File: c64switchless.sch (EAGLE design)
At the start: 12 parts, among them IC1 27C256, IC2 PIC12F629P

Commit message: hole sizes
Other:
- note added: "Rev 1.12"
- note removed: "Rev 1.11"
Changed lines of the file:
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@@
 <text x="165.1" y="17.78" size="1.778" layer="91">adapter with switchless multikernal switch</text>
 <text x="165.1" y="12.7" size="1.778" layer="91">Design by BWACK</text>
-<text x="246.634" y="5.334" size="1.778" layer="91">Rev 1.11</text>
+<text x="246.634" y="5.334" size="1.778" layer="91">Rev 1.12</text>
 <text x="165.1" y="5.08" size="1.778" layer="91">http://www.ohwr.org/</text>
 <text x="165.1" y="7.62" size="1.778" layer="91">CERN OPEN HARDWARE LICENSE v1.2</text>

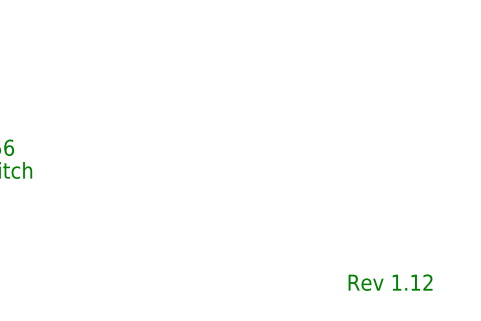
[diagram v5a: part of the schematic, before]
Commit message: Rev 1.13
Moved IC2 to clear space for the socket in the C64.
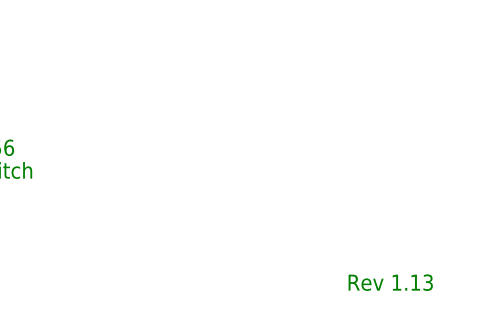
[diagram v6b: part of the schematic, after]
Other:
- note added: "Rev 1.13"
- note removed: "Rev 1.12"
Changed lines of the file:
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@@
 <text x="165.1" y="17.78" size="1.778" layer="91">adapter with switchless multikernal switch</text>
 <text x="165.1" y="12.7" size="1.778" layer="91">Design by BWACK</text>
-<text x="246.634" y="5.334" size="1.778" layer="91">Rev 1.12</text>
+<text x="246.634" y="5.334" size="1.778" layer="91">Rev 1.13</text>
 <text x="165.1" y="5.08" size="1.778" layer="91">http://www.ohwr.org/</text>
 <text x="165.1" y="7.62" size="1.778" layer="91">CERN OPEN HARDWARE LICENSE v1.2</text>

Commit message: resistor values
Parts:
- R1: value 2k -> 1k
- R2: value 2k -> 3k3
- R3: value 2k -> 560R
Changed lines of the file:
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@@
 <part name="GND5" library="supply1" deviceset="GND" device=""/>
 <part name="GND6" library="supply1" deviceset="GND" device=""/>
-<part name="R1" library="rcl" deviceset="R-EU_" device="0207/10" value="2k"/>
-<part name="R2" library="rcl" deviceset="R-EU_" device="0207/10" value="2k"/>
-<part name="R3" library="rcl" deviceset="R-EU_" device="0207/10" value="2k"/>
+<part name="R1" library="rcl" deviceset="R-EU_" device="0207/10" value="1k"/>
+<part name="R2" library="rcl" deviceset="R-EU_" device="0207/10" value="3k3"/>
+<part name="R3" library="rcl" deviceset="R-EU_" device="0207/10" value="560R"/>
 <part name="P+1" library="supply1" deviceset="VCC" device=""/>
 <part name="C1" library="rcl" deviceset="C-EU" device="025-024X044" value="100n"/>
